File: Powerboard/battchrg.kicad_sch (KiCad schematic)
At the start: 62 parts, among them J1 Thermistor Connection, Q1 SI7617DN-T1-GE3, Q2 SI7617DN-T1-GE3, Q3 SI7617DN-T1-GE3, Q4 SIS412DN-T1-GE3-iclr, Q5 SIS412DN-T1-GE3-iclr

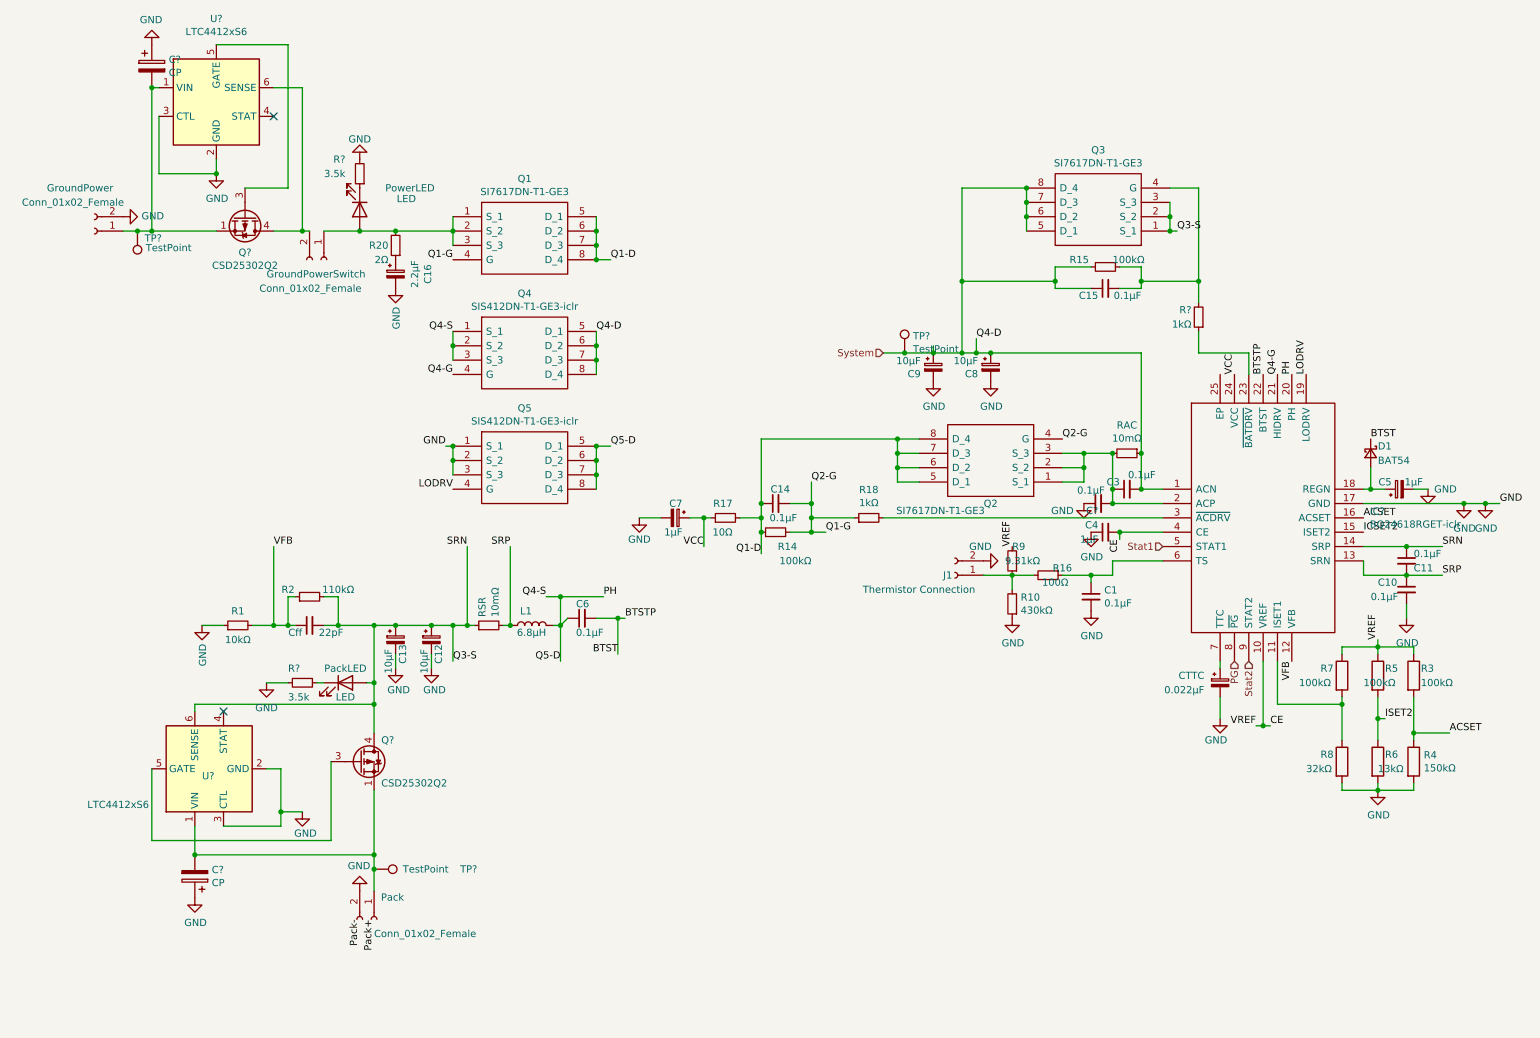
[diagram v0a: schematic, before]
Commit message: added vbus to 3.3v converter
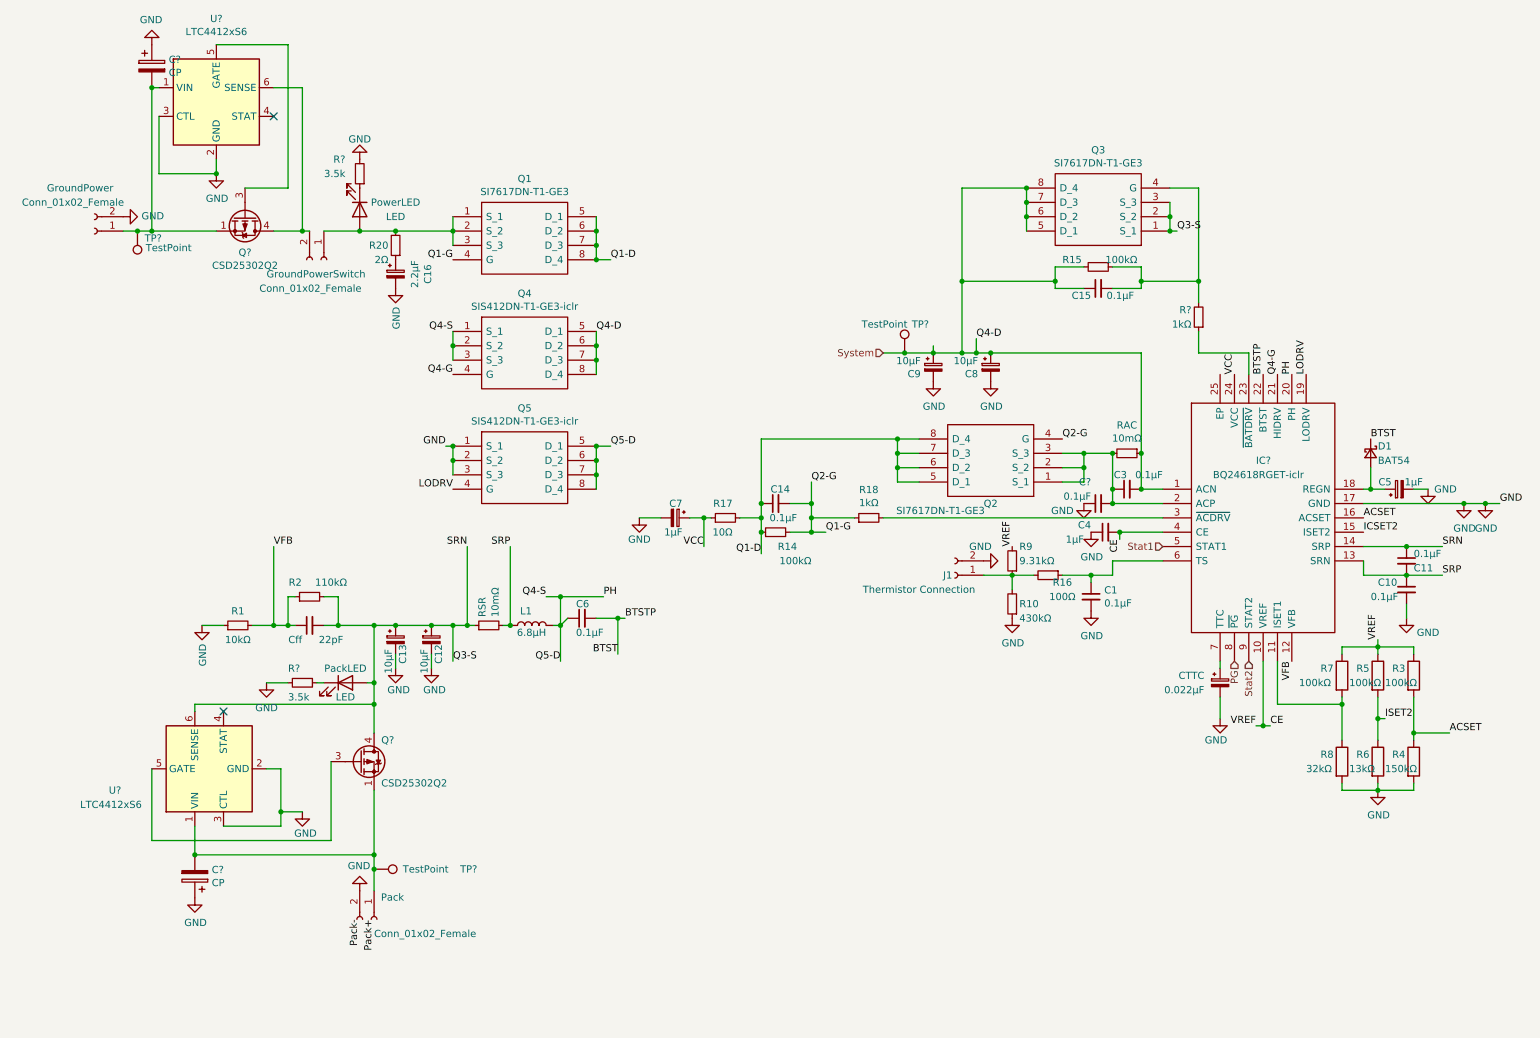
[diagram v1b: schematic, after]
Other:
- moved on the sheet: C15, R15

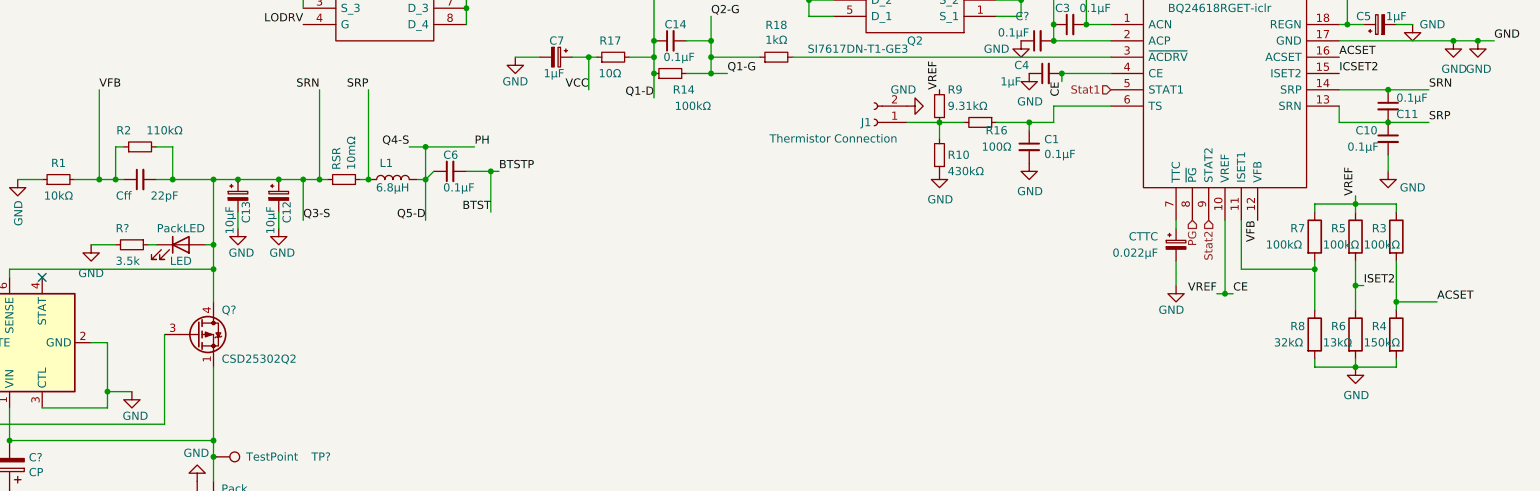
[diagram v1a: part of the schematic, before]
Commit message: Checked the values for battery monitor
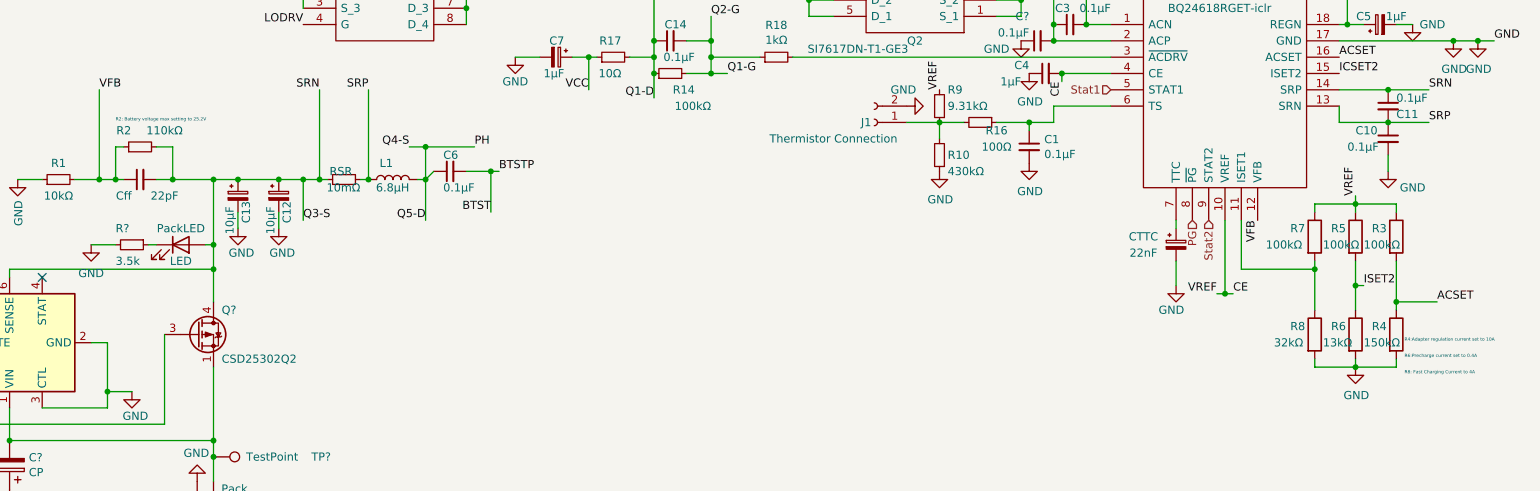
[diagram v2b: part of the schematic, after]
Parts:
- CTTC: value 0.022µF -> 22nF
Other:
- note added: "R2: Battery voltage max setting to 25.2V"
- note added: "R4:Adapter regulation current set to 10A"
- note added: "R6:Precharge current set to 0.4A"
- note added: "R8: Fast Charging Current to 4A"
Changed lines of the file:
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@@
     (stroke (width 0) (type default) (color 0 0 0 0))
+  )
+  (text "R2: Battery voltage max setting to 25.2V\n" (at 54.61 118.11 0)
+    (effects (font (size 0.5 0.5)) (justify left bottom))
+  )
+  (text "R4:Adapter regulation current set to 10A" (at 255.27 152.4 0)
+    (effects (font (size 0.5 0.5)) (justify left bottom))
+  )
+  (text "R8: Fast Charging Current to 4A" (at 255.27 157.48 0)
+    (effects (font (size 0.5 0.5)) (justify left bottom))
+  )
+  (text "R6:Precharge current set to 0.4A" (at 255.27 154.94 0)
+    (effects (font (size 0.5 0.5)) (justify left bottom))
   )
   (label "Q5-D" (at 111.76 95.25 0)
@@
     (in_bom yes) (on_board yes)
     (property "Reference" "CTTC" (id 0) (at 214.63 135.89 0))
-    (property "Value" "0.022µF" (id 1) (at 213.36 138.43 0))
+    (property "Value" "22nF" (id 1) (at 214.63 138.43 0))
     (property "Footprint" "" (id 2) (at 219.71 137.16 0)
       (effects (font (size 1.27 1.27)) hide)
@@
   (symbol (lib_id "Device:R_Small") (at 90.17 127 90) (unit 1)
     (in_bom yes) (on_board yes)
-    (property "Reference" "RSR" (id 0) (at 89.0016 125.5014 0)
-      (effects (font (size 1.27 1.27)) (justify left))
-    )
-    (property "Value" "10mΩ" (id 1) (at 91.313 125.5014 0)
-      (effects (font (size 1.27 1.27)) (justify left))
-    )
+    (property "Reference" "RSR" (id 0) (at 91.44 125.73 90)
+      (effects (font (size 1.27 1.27)) (justify left))
+    )
+    (property "Value" "10mΩ" (id 1) (at 92.71 128.27 90)
+      (effects (font (size 1.27 1.27)) (justify left))
+    )

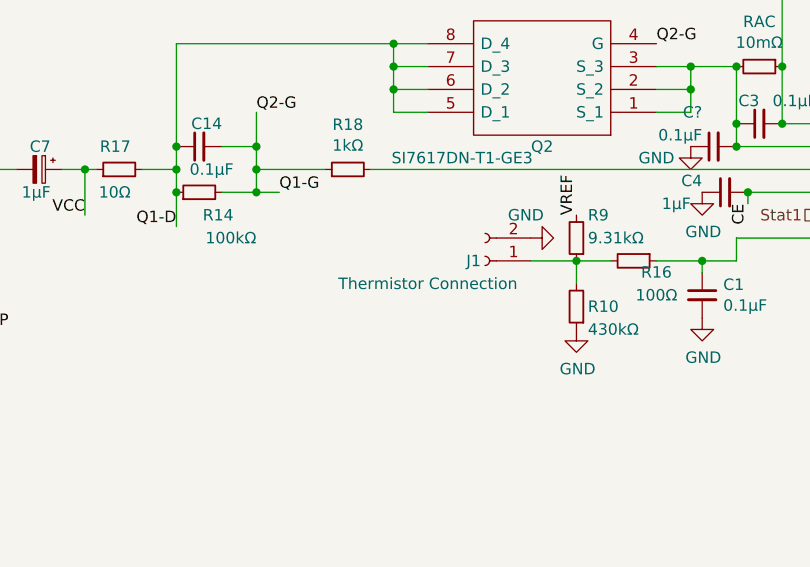
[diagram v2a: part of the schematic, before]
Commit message: Added thermistor resistor for specific thermistor
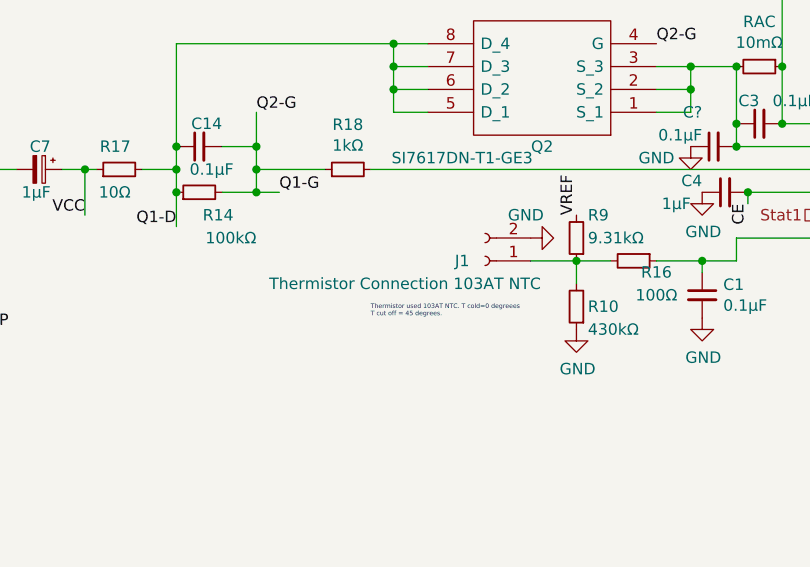
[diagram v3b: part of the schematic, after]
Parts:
- J1: value Thermistor Connection -> Thermistor Connection 103AT NTC
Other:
- note added: "Thermistor used 103AT NTC. T cold=0 degreees T cut off = 45 degrees."
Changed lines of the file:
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@@
+    (effects (font (size 0.5 0.5)) (justify left bottom))
+  )
+  (text "Thermistor used 103AT NTC. T cold=0 degreees\nT cut off = 45 degrees. \n"
+    (at 160.02 124.46 0)
     (effects (font (size 0.5 0.5)) (justify left bottom))
   )
@@
   (symbol (lib_id "Connector:Conn_01x02_Female") (at 172.72 118.11 180) (unit 1)
     (in_bom yes) (on_board yes)
-    (property "Reference" "J1" (id 0) (at 171.45 118.11 0))
-    (property "Value" "Thermistor Connection" (id 1) (at 166.37 120.65 0))
+    (property "Reference" "J1" (id 0) (at 170.18 118.11 0))
+    (property "Value" "Thermistor Connection 103AT NTC" (id 1) (at 163.83 120.65 0))
     (property "Footprint" "" (id 2) (at 172.72 118.11 0)
       (effects (font (size 1.27 1.27)) hide)

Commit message: isolation switch added
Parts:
- removed GroundPowerSwitch: Conn_01x02_Female, symbol Connector:Conn_01x02_Female
- added J?: IsolationSwitch, symbol Connector:Conn_01x02_Female
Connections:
- net at PowerLED.2 (A), Q1.1 (S_1), Q1.2 (S_2)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: now also Q?.4 (D), Q?.7 (D), U?.6 (SENSE)
- net at C?.2, Q?.1 (S), Q?.2 (S)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: now also J?.1 (Pin_1); no longer Pack.1 (Pin_1), TP?.1
- new net: J?.2 (Pin_2), Pack.1 (Pin_1), TP?.1
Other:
- moved on the sheet: Pack, TP?
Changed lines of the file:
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@@
   (junction (at 210.82 57.15) (diameter 0) (color 0 0 0 0)
   )
+  (junction (at 69.85 177.038) (diameter 0) (color 0 0 0 0)
+  )
   (junction (at 254 146.05) (diameter 0) (color 0 0 0 0)
   )
@@
   )
   (junction (at 109.22 100.33) (diameter 0) (color 0 0 0 0)
-  )
-  (junction (at 69.85 170.18) (diameter 0) (color 0 0 0 0)
   )
   (junction (at 113.03 125.73) (diameter 0) (color 0 0 0 0)
@@
     (stroke (width 0) (type default) (color 0 0 0 0))
   )
-  (wire (pts (xy 57.15 57.15) (xy 58.42 57.15))
-    (stroke (width 0) (type default) (color 0 0 0 0))
-  )
   (wire (pts (xy 30.48 31.75) (xy 30.48 57.15))
     (stroke (width 0) (type default) (color 0 0 0 0))
@@
     (stroke (width 0) (type default) (color 0 0 0 0))
   )
+  (wire (pts (xy 69.85 172.72) (xy 69.85 177.038))
+    (stroke (width 0) (type default) (color 0 0 0 0))
+  )
   (wire (pts (xy 176.53 76.2) (xy 176.53 78.74))
     (stroke (width 0) (type default) (color 0 0 0 0))
@@
     (stroke (width 0) (type default) (color 0 0 0 0))
   )
-  (wire (pts (xy 60.96 57.15) (xy 67.31 57.15))
+  (wire (pts (xy 57.15 57.15) (xy 67.31 57.15))
     (stroke (width 0) (type default) (color 0 0 0 0))
   )
@@
     (stroke (width 0) (type default) (color 0 0 0 0))
   )
-  (wire (pts (xy 69.85 170.18) (xy 69.85 173.99))
+  (wire (pts (xy 69.85 177.038) (xy 69.85 180.848))
     (stroke (width 0) (type default) (color 0 0 0 0))
   )
@@
     (effects (font (size 1.27 1.27)) (justify right bottom))
   )
-  (label "Pack+" (at 69.85 179.07 270)
+  (label "Pack+" (at 69.85 185.928 270)
     (effects (font (size 1.27 1.27)) (justify right bottom))
   )
@@
     (effects (font (size 1.27 1.27)) (justify left bottom))
   )
-  (label "Pack-" (at 67.31 179.07 270)
+  (label "Pack-" (at 67.31 185.928 270)
     (effects (font (size 1.27 1.27)) (justify right bottom))
   )
@@
     (pin "2")
   )
-  (symbol (lib_id "Connector:Conn_01x02_Female") (at 69.85 179.07 270) (unit 1)
-    (in_bom yes) (on_board yes)
-    (property "Reference" "Pack" (id 0) (at 71.0692 175.1584 90)
-      (effects (font (size 1.27 1.27)) (justify left))
-    )
-    (property "Value" "Conn_01x02_Female" (id 1) (at 69.85 181.61 90)
-      (effects (font (size 1.27 1.27)) (justify left))
-    )
-    (property "Footprint" "" (id 2) (at 69.85 179.07 0)
-      (effects (font (size 1.27 1.27)) hide)
-    )
-    (property "Datasheet" "~" (id 3) (at 69.85 179.07 0)
-      (effects (font (size 1.27 1.27)) hide)
-    )
-    (pin "1")
-    (pin "2")
-  )
-  (symbol (lib_id "power:GND") (at 67.31 173.99 180) (unit 1)
-    (in_bom yes) (on_board yes)
-    (property "Reference" "#PWR?" (id 0) (at 67.31 167.64 0)
-      (effects (font (size 1.27 1.27)) hide)
-    )
-    (property "Value" "GND" (id 1) (at 67.183 169.5958 0))
-    (property "Footprint" "" (id 2) (at 67.31 173.99 0)
-      (effects (font (size 1.27 1.27)) hide)
-    )
-    (property "Datasheet" "" (id 3) (at 67.31 173.99 0)
+  (symbol (lib_id "Connector:Conn_01x02_Female") (at 69.85 185.928 270) (unit 1)
+    (in_bom yes) (on_board yes)
+    (property "Reference" "Pack" (id 0) (at 71.0692 182.0164 90)
+      (effects (font (size 1.27 1.27)) (justify left))
+    )
+    (property "Value" "Conn_01x02_Female" (id 1) (at 69.85 188.468 90)
+      (effects (font (size 1.27 1.27)) (justify left))
+    )
+    (property "Footprint" "" (id 2) (at 69.85 185.928 0)
+      (effects (font (size 1.27 1.27)) hide)
+    )
+    (property "Datasheet" "~" (id 3) (at 69.85 185.928 0)
+      (effects (font (size 1.27 1.27)) hide)
+    )
+    (pin "1")
+    (pin "2")
+  )
+  (symbol (lib_id "power:GND") (at 67.31 180.848 180) (unit 1)
+    (in_bom yes) (on_board yes)
+    (property "Reference" "#PWR?" (id 0) (at 67.31 174.498 0)
+      (effects (font (size 1.27 1.27)) hide)
+    )
+    (property "Value" "GND" (id 1) (at 67.183 176.4538 0))
+    (property "Footprint" "" (id 2) (at 67.31 180.848 0)
+      (effects (font (size 1.27 1.27)) hide)
+    )
+    (property "Datasheet" "" (id 3) (at 67.31 180.848 0)
       (effects (font (size 1.27 1.27)) hide)
     )
@@
     (pin "8")
   )
-  (symbol (lib_id "Connector:Conn_01x02_Female") (at 60.96 62.23 270) (unit 1)
-    (in_bom yes) (on_board yes)
-    (property "Reference" "GroundPowerSwitch" (id 0) (at 50.8 64.77 90)
-      (effects (font (size 1.27 1.27)) (justify left))
-    )
-    (property "Value" "Conn_01x02_Female" (id 1) (at 49.53 67.31 90)
-      (effects (font (size 1.27 1.27)) (justify left))
-    )
-    (property "Footprint" "" (id 2) (at 60.96 62.23 0)
-      (effects (font (size 1.27 1.27)) hide)
-    )
-    (property "Datasheet" "~" (id 3) (at 60.96 62.23 0)
-      (effects (font (size 1.27 1.27)) hide)
-    )
-    (pin "1")
-    (pin "2")
-  )
   (symbol (lib_id "Connector:TestPoint") (at 27.94 57.15 180) (unit 1)
     (in_bom yes) (on_board yes)
@@
     (pin "1")
   )
-  (symbol (lib_id "Connector:TestPoint") (at 69.85 170.18 270) (unit 1)
-    (in_bom yes) (on_board yes)
-    (property "Reference" "TP?" (id 0) (at 85.09 170.18 90)
-      (effects (font (size 1.27 1.27)) (justify left))
-    )
-    (property "Value" "TestPoint" (id 1) (at 74.93 170.18 90)
-      (effects (font (size 1.27 1.27)) (justify left))
-    )
-    (property "Footprint" "" (id 2) (at 69.85 175.26 0)
-      (effects (font (size 1.27 1.27)) hide)
-    )
-    (property "Datasheet" "~" (id 3) (at 69.85 175.26 0)
+  (symbol (lib_id "Connector:TestPoint") (at 69.85 177.038 270) (unit 1)
+    (in_bom yes) (on_board yes)
+    (property "Reference" "TP?" (id 0) (at 85.09 177.038 90)
+      (effects (font (size 1.27 1.27)) (justify left))
+    )
+    (property "Value" "TestPoint" (id 1) (at 74.93 177.038 90)
+      (effects (font (size 1.27 1.27)) (justify left))
+    )
+    (property "Footprint" "" (id 2) (at 69.85 182.118 0)
+      (effects (font (size 1.27 1.27)) hide)
+    )
+    (property "Datasheet" "~" (id 3) (at 69.85 182.118 0)
       (effects (font (size 1.27 1.27)) hide)
     )
@@
       (effects (font (size 1.27 1.27)) hide)
     )
+    (pin "1")
+    (pin "2")
+  )
+  (symbol (lib_id "Connector:Conn_01x02_Female") (at 74.93 170.18 0) (unit 1)
+    (in_bom yes) (on_board yes) (fields_autoplaced)
+    (property "Reference" "J?" (id 0) (at 75.6412 170.6153 0)
+      (effects (font (size 1.27 1.27)) (justify left))
+    )
+    (property "Value" "IsolationSwitch" (id 1) (at 75.6412 173.1522 0)
+      (effects (font (size 1.27 1.27)) (justify left))
+    )
+    (property "Footprint" "" (id 2) (at 74.93 170.18 0)
+      (effects (font (size 1.27 1.27)) hide)
+    )
+    (property "Datasheet" "~" (id 3) (at 74.93 170.18 0)
+      (effects (font (size 1.27 1.27)) hide)
+    )
